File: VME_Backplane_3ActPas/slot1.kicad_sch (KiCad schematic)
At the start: 7 parts, among them X101 DIN41612_03x32_ABC_VMEbus, X401A1 Jumper_2_Open, X401B1 Jumper_2_Open, X401C1 Jumper_2_Open, X401D1 Jumper_2_Open, X501 Jumper_2_Open

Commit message: Rename sheets to reflect their slots
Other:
- title: SOCKET 1 -> SLOT 1
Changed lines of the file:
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@@
   (paper "A4")
   (title_block
-    (title "SOCKET 1")
-    (date "2023-10-10")
+    (title "SLOT 1")
+    (date "2024-01-02")
     (rev "1")
     (company "(C) TOM STOREY")
@@
   (symbol (lib_id "power:+12V") (at 55.88 137.16 0) (unit 1)
     (in_bom yes) (on_board yes) (fields_autoplaced)
-    (property "Reference" "#PWR0120" (id 0) (at 55.88 140.97 0)
+    (property "Reference" "#PWR?" (id 0) (at 55.88 140.97 0)
       (effects (font (size 1.27 1.27)) hide)
     )
@@
   (symbol (lib_id "power:+BATT") (at 55.88 124.46 0) (unit 1)
     (in_bom yes) (on_board yes) (fields_autoplaced)
-    (property "Reference" "#PWR0119" (id 0) (at 55.88 128.27 0)
+    (property "Reference" "#PWR?" (id 0) (at 55.88 128.27 0)
       (effects (font (size 1.27 1.27)) hide)
     )
@@
   (symbol (lib_id "power:GND") (at 55.88 165.1 0) (unit 1)
     (in_bom yes) (on_board yes) (fields_autoplaced)
-    (property "Reference" "#PWR0121" (id 0) (at 55.88 171.45 0)
+    (property "Reference" "#PWR?" (id 0) (at 55.88 171.45 0)
       (effects (font (size 1.27 1.27)) hide)
     )
@@
   (symbol (lib_id "power:+5V") (at 55.88 149.86 0) (unit 1)
     (in_bom yes) (on_board yes) (fields_autoplaced)
-    (property "Reference" "#PWR0118" (id 0) (at 55.88 153.67 0)
+    (property "Reference" "#PWR?" (id 0) (at 55.88 153.67 0)
       (effects (font (size 1.27 1.27)) hide)
     )
@@
   (symbol (lib_id "power:-12V") (at 55.88 177.8 180) (unit 1)
     (in_bom yes) (on_board yes) (fields_autoplaced)
-    (property "Reference" "#PWR0122" (id 0) (at 55.88 180.34 0)
-      (effects (font (size 1.27 1.27)) hide)
-    )
+    (property "Reference" "#PWR?" (id 0) (at 55.88 180.34 0)
+      (effects (font (size 1.27 1.27)) hide)
+    )

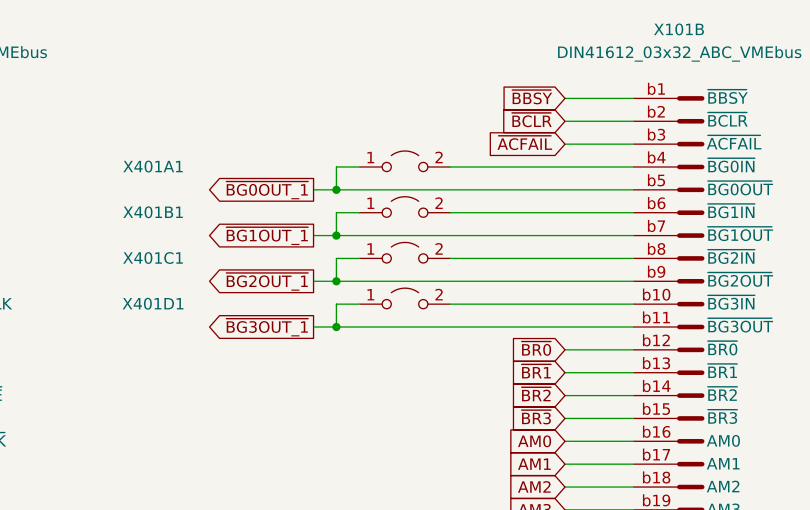
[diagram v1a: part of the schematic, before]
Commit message: Change to own DIN 41612 footprint with 3D model
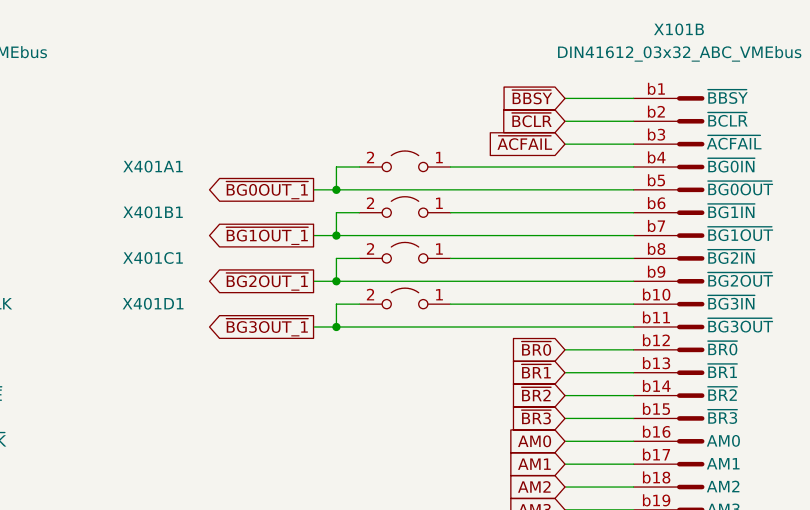
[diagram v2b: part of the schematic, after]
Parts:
- X101: footprint Connector_DIN:DIN41612_C_3x32_Male_Horizontal_THT -> COMET footprints:Connector_DIN41612_C_3x32_Female_Vertical_THT
- X101: footprint Connector_DIN:DIN41612_C_3x32_Female_Vertical_THT -> COMET footprints:Connector_DIN41612_C_3x32_Female_Vertical_THT
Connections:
- net ~{BG0OUT_1}: now also X401A1.2 (B); no longer X401A1.1 (A)
- net ~{BG1OUT_1}: now also X401B1.2 (B); no longer X401B1.1 (A)
- net ~{BG2OUT_1}: now also X401C1.2 (B); no longer X401C1.1 (A)
- net ~{BG3OUT_1}: now also X401D1.2 (B); no longer X401D1.1 (A)
- net at X101.b6 (~{BG1IN}): now also X401B1.1 (A); no longer X401B1.2 (B)
- net at X101.b8 (~{BG2IN}): now also X401C1.1 (A); no longer X401C1.2 (B)
- net at X101.b4 (~{BG0IN}): now also X401A1.1 (A); no longer X401A1.2 (B)
- net at X101.b10 (~{BG3IN}): now also X401D1.1 (A); no longer X401D1.2 (B)
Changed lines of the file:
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@@
   (symbol (lib_id "power:+12V") (at 55.88 137.16 0) (unit 1)
     (in_bom yes) (on_board yes) (fields_autoplaced)
-    (property "Reference" "#PWR?" (id 0) (at 55.88 140.97 0)
+    (property "Reference" "#PWR0121" (id 0) (at 55.88 140.97 0)
       (effects (font (size 1.27 1.27)) hide)
     )
@@
     (pin "1")
   )
-  (symbol (lib_id "Jumper:Jumper_2_Open") (at 147.32 50.8 0) (unit 1)
+  (symbol (lib_id "Jumper:Jumper_2_Open") (at 147.32 50.8 0) (mirror y) (unit 1)
     (in_bom yes) (on_board yes)
     (property "Reference" "X401B1" (id 0) (at 119.38 50.8 0))
@@
     (pin "2")
   )
-  (symbol (lib_id "Jumper:Jumper_2_Open") (at 147.32 55.88 0) (unit 1)
+  (symbol (lib_id "Jumper:Jumper_2_Open") (at 147.32 55.88 0) (mirror y) (unit 1)
     (in_bom yes) (on_board yes)
     (property "Reference" "X401C1" (id 0) (at 119.38 55.88 0))
@@
   (symbol (lib_id "power:+BATT") (at 55.88 124.46 0) (unit 1)
     (in_bom yes) (on_board yes) (fields_autoplaced)
-    (property "Reference" "#PWR?" (id 0) (at 55.88 128.27 0)
+    (property "Reference" "#PWR0122" (id 0) (at 55.88 128.27 0)
       (effects (font (size 1.27 1.27)) hide)
     )
@@
   (symbol (lib_id "power:GND") (at 55.88 165.1 0) (unit 1)
     (in_bom yes) (on_board yes) (fields_autoplaced)
-    (property "Reference" "#PWR?" (id 0) (at 55.88 171.45 0)
+    (property "Reference" "#PWR0124" (id 0) (at 55.88 171.45 0)
       (effects (font (size 1.27 1.27)) hide)
     )
@@
     (property "Reference" "X101" (id 0) (at 231.14 30.48 0))
     (property "Value" "DIN41612_03x32_ABC_VMEbus" (id 1) (at 231.14 33.02 0))
-    (property "Footprint" "Connector_DIN:DIN41612_C_3x32_Male_Horizontal_THT" (id 2) (at 233.68 76.2 0)
+    (property "Footprint" "COMET footprints:Connector_DIN41612_C_3x32_Female_Vertical_THT" (id 2) (at 233.68 76.2 0)
       (effects (font (size 1.27 1.27)) hide)
     )
@@
     (pin "c9")
   )
-  (symbol (lib_id "Jumper:Jumper_2_Open") (at 147.32 45.72 0) (unit 1)
+  (symbol (lib_id "Jumper:Jumper_2_Open") (at 147.32 45.72 0) (mirror y) (unit 1)
     (in_bom yes) (on_board yes)
     (property "Reference" "X401A1" (id 0) (at 119.38 45.72 0))
@@
     (property "Reference" "X101" (id 0) (at 93.98 30.48 0))
     (property "Value" "DIN41612_03x32_ABC_VMEbus" (id 1) (at 93.98 33.02 0))
-    (property "Footprint" "Connector_DIN:DIN41612_C_3x32_Female_Vertical_THT" (id 2) (at 96.52 76.2 0)
+    (property "Footprint" "COMET footprints:Connector_DIN41612_C_3x32_Female_Vertical_THT" (id 2) (at 96.52 76.2 0)
       (effects (font (size 1.27 1.27)) hide)
     )
@@
   (symbol (lib_id "power:+5V") (at 55.88 149.86 0) (unit 1)
     (in_bom yes) (on_board yes) (fields_autoplaced)
-    (property "Reference" "#PWR?" (id 0) (at 55.88 153.67 0)
+    (property "Reference" "#PWR0123" (id 0) (at 55.88 153.67 0)
       (effects (font (size 1.27 1.27)) hide)
     )
@@
     (pin "1")
   )
-  (symbol (lib_id "Jumper:Jumper_2_Open") (at 147.32 60.96 0) (unit 1)
+  (symbol (lib_id "Jumper:Jumper_2_Open") (at 147.32 60.96 0) (mirror y) (unit 1)
     (in_bom yes) (on_board yes)
     (property "Reference" "X401D1" (id 0) (at 119.38 60.96 0))
@@
     (property "Reference" "X101" (id 0) (at 177.8 30.48 0))
     (property "Value" "DIN41612_03x32_ABC_VMEbus" (id 1) (at 177.8 33.02 0))
-    (property "Footprint" "Connector_DIN:DIN41612_C_3x32_Male_Horizontal_THT" (id 2) (at 180.34 76.2 0)
+    (property "Footprint" "COMET footprints:Connector_DIN41612_C_3x32_Female_Vertical_THT" (id 2) (at 180.34 76.2 0)
       (effects (font (size 1.27 1.27)) hide)
     )
@@
   (symbol (lib_id "power:-12V") (at 55.88 177.8 180) (unit 1)
     (in_bom yes) (on_board yes) (fields_autoplaced)
-    (property "Reference" "#PWR?" (id 0) (at 55.88 180.34 0)
-      (effects (font (size 1.27 1.27)) hide)
-    )
+    (property "Reference" "#PWR0125" (id 0) (at 55.88 180.34 0)
+      (effects (font (size 1.27 1.27)) hide)
+    )

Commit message: Add/update revision information in schematics and PCB
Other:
- company: (C) TOM STOREY -> TOM STOREY
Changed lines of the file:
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@@
   (title_block
     (title "SLOT 1")
-    (date "2024-01-02")
+    (date "2024-01-03")
     (rev "1")
-    (company "(C) TOM STOREY")
+    (company "TOM STOREY")
     (comment 1 "FREE FOR NON-COMMERCIAL USE")
   )
